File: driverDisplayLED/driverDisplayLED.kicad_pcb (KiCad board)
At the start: 2 copper layers, 59 parts, among them J1 Conn_01x12_Male, J10 Conn_01x12_Male, J11 Conn_01x12_Male, J12 Conn_01x12_Male, J13 Conn_01x12_Male, J14 Conn_01x12_Male, J15 Conn_01x12_Male, J16 Conn_01x12_Male, J17 Conn_01x12_Male, J2 Conn_01x12_Male, J3 Conn_01x12_Male, J4 Conn_02x08_Counter_Clockwise, J5 Conn_01x12_Male, J6 Conn_01x12_Male, J7 Conn_01x12_Male, J8 Conn_01x12_Male, J9 Conn_01x12_Male, Q1 FDS4953, Q2 FDS4953, Q3 FDS4953, Q4 FDS4953, Q5 FDS4953, Q6 FDS4953, Q7 FDS4953, Q8 FDS4953, U1 74HC245, U2 74HC595, U3 74HC595, U4 74HC245, U5 74HC138D, U6 74HC04, U7 74HC595, U8 74HC595, U9 74HC138D

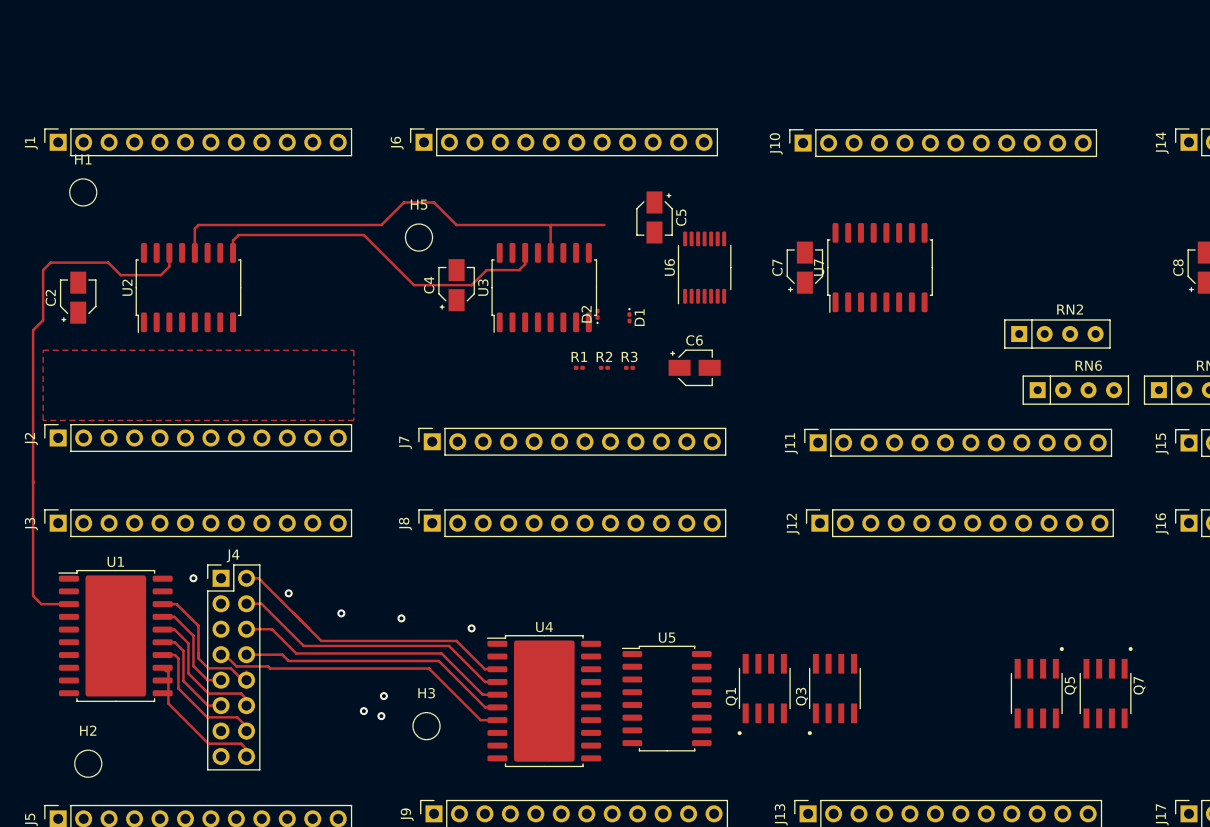
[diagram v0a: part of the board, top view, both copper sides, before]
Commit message: footprint matrix + vias primer bloque
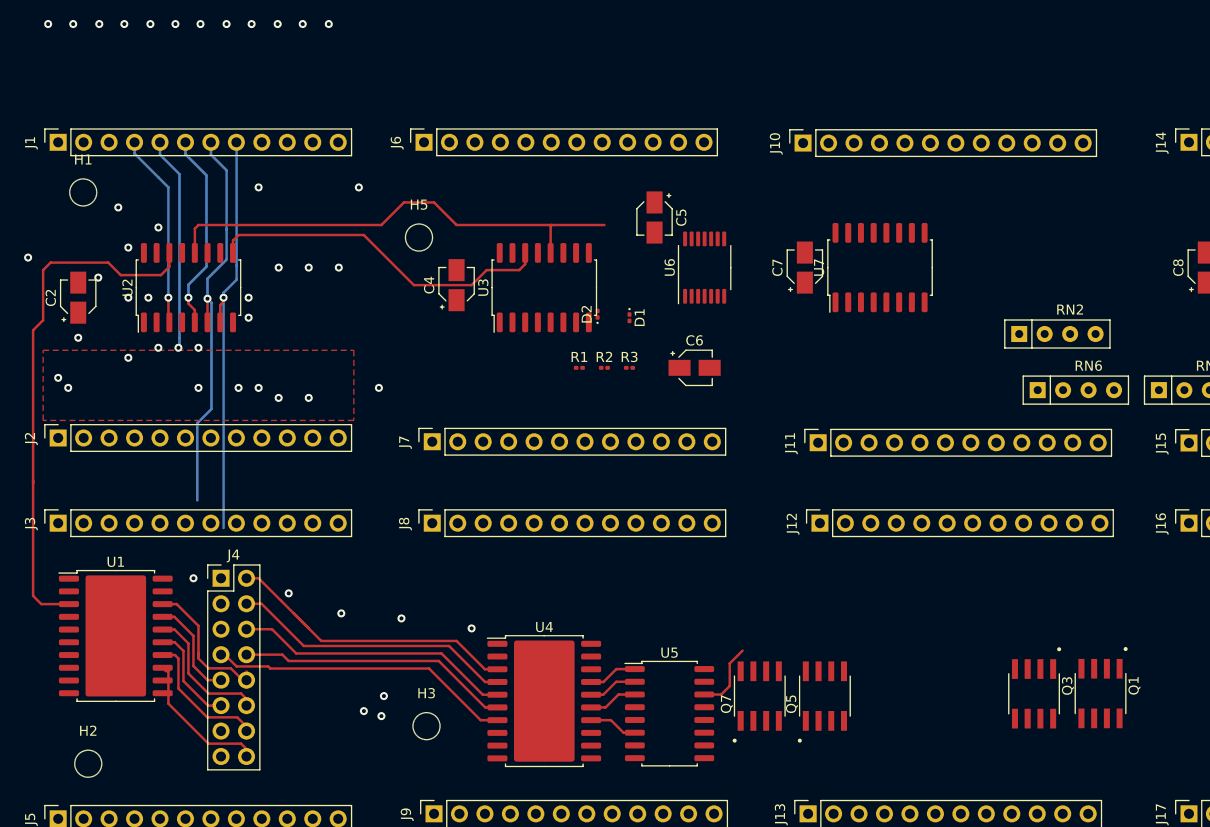
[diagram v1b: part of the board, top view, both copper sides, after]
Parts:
- moved Q7 34.5 mm to (133.0, 117.8), turned to 90 degrees
- moved Q1 33.5 mm to (167.0, 117.5), turned to 270 degrees
- moved Q5 21.1 mm to (139.5, 117.8), turned to 90 degrees
- moved Q3 19.9 mm to (160.4, 117.5), turned to 270 degrees
- moved U5 1.52 mm to (124.0, 119.5)
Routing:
- net /L1R1: track 0.00 -> 41.6 mm, vias 0 -> 2
- net /L1R2: track 0.00 -> 40.3 mm, vias 0 -> 1
- net /L1R4: track 0.00 -> 21.3 mm, vias 0 -> 2
- net /L1R3: track 0.00 -> 19.8 mm, vias 0 -> 2
- net /L1R5: track 0.00 -> 19.4 mm, vias 0 -> 2
- net /Y1-G1b: track 0.00 -> 6.95 mm
- net Net-(U4-Pad15): track 0.00 -> 4.90 mm
- net Net-(U4-Pad17): track 0.00 -> 4.90 mm
- net Net-(U4-Pad16): track 0.00 -> 4.90 mm
- net Net-(U4-Pad14): track 0.00 -> 4.88 mm
- net /L1R8: vias 0 -> 1
- net /L1R7: vias 0 -> 1
- net /L1R6: vias 0 -> 1
- net /H4a: vias 0 -> 1
- net /H3a: vias 0 -> 1
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
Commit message: Esquemático actualizado, encapsulados de capacitores actualizados, footprints de prueba de las matrices led, vias
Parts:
- added J19: Conn_01x02_Female, Connector_Phoenix_MC:PhoenixContact_MCV_1,5_2-GF-3.5_1x02_P3.50mm_Vertical_ThreadedFlange_MountHole, F.Cu at (218.0, 109.0)
- added L1: LedMatrix_M, myLedMatrixFootprint:1588AB-24, F.Cu at (204.2, 98.2)
- added L2: LedMatrix_M, myLedMatrixFootprint:1588AB-24, F.Cu at (243.2, 59.2)
- added L3: LedMatrix_M, myLedMatrixFootprint:1588AB-24, F.Cu at (243.2, 98.2)
- added L4: LedMatrix_M, myLedMatrixFootprint:1588AB-24, F.Cu at (282.1, 59.2)
- added L5: LedMatrix_M, myLedMatrixFootprint:1588AB-24, F.Cu at (204.2, 59.2)
- added L6: LedMatrix_M, myLedMatrixFootprint:1588AB-24, F.Cu at (321.0, 98.2)
- added L7: LedMatrix_M, myLedMatrixFootprint:1588AB-24, F.Cu at (321.0, 59.2)
- added L8: LedMatrix_M, myLedMatrixFootprint:1588AB-24, F.Cu at (282.1, 98.2)
- added U10: 74HC04, Package_SO:TSSOP-14_4.4x5mm_P0.65mm, F.Cu at (207.9, 139.6)
- C1, C11, C2, C3, C4, C5, C6, C7, C8: footprint Capacitor_SMD:CP_Elec_3x5.3 -> Capacitor_SMD:C_0201_0603Metric
- moved C5 112.5 mm to (207.4, 143.7), turned to 0 degrees
- moved R1 111.6 mm to (209.9, 143.7)
- moved R2 111.5 mm to (212.3, 143.7)
- moved R3 111.5 mm to (214.8, 143.7)
- moved U6 110.1 mm to (216.6, 139.6), turned to 0 degrees
- moved D2 109.0 mm to (205.0, 143.7), turned to 0 degrees
- moved C6 108.1 mm to (217.2, 143.7)
- moved D1 107.3 mm to (205.0, 145.5), turned to 0 degrees
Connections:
- D1 pad 2: Net-(D1-Pad2) -> GND
- R1 pad 2: Net-(D1-Pad2) -> Net-(J4-Pad2)
- R2 pad 1: Net-(C6-Pad1) -> Net-(R1-Pad1)
- R2 pad 2: Net-(R1-Pad1) -> GND
- R3 pad 2: Net-(D1-Pad2) -> GND
- U1 pad 8: Net-(RN2-Pad5) -> Net-(RN2-Pad2)
- U6 pad 1: Net-(C6-Pad1) -> (no net)
- U6 pad 2: Net-(C5-Pad1) -> (no net)
- U6 pad 3: Net-(C6-Pad1) -> (no net)
- U6 pad 4: /E1 -> (no net)
- U6 pad 5: /E1 -> (no net)
- U6 pad 6: /E3 -> (no net)
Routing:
- net /L1R6: track 0.00 -> 21.2 mm, vias 1 -> 2
- net /L1R7: track 0.00 -> 10.2 mm, vias 1 -> 2
- net /L1R5: track 19.4 -> 25.4 mm
- net (no net): vias 46 -> 44

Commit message: place and route++
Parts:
- removed U6: 74HC04, Package_SO:TSSOP-14_4.4x5mm_P0.65mm
- U10: footprint Package_SO:TSSOP-14_4.4x5mm_P0.65mm -> Package_SO:SO-14_5.3x10.2mm_P1.27mm
- moved L5 216.4 mm to (-12.0, 68.0)
- moved D1 108.0 mm to (120.7, 78.0), turned to 270 degrees
- moved C6 107.1 mm to (127.8, 84.7)
- moved R2 107.1 mm to (122.9, 84.7)
- moved R1 107.1 mm to (120.5, 84.7)
- moved R3 107.1 mm to (125.4, 84.7)
- moved C5 105.8 mm to (124.5, 78.0), turned to 270 degrees
- moved D2 105.5 mm to (122.5, 78.0), turned to 270 degrees
- moved U10 99.0 mm to (132.2, 75.8), turned to 90 degrees
- moved U7 5.62 mm to (150.6, 75.5)
- moved J1 1.45 mm to (63.1, 64.0)
- moved J10 1.25 mm to (137.3, 63.8)
- moved J14 1.25 mm to (175.8, 63.8)
- moved J6 1.25 mm to (99.5, 63.8)
- moved J11 1.00 mm to (138.8, 91.5)
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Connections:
- U10 pad 14: (no net) -> VCC
- U10 pad 7: (no net) -> GND
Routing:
- net (no net): track 0.00 -> 624.2 mm
- net /H5a: track 0.00 -> 147.2 mm, vias 0 -> 6
- net /H6a: track 0.00 -> 140.0 mm, vias 0 -> 6
- net /H7a: track 0.00 -> 132.5 mm, vias 0 -> 6
- net /H2a: track 0.00 -> 129.8 mm, vias 1 -> 0
- net /H4b: track 0.00 -> 127.4 mm
- net /H2b: track 0.00 -> 126.2 mm
- net /H4a: track 0.00 -> 124.8 mm, vias 1 -> 0
- net /H8a: track 0.00 -> 124.7 mm
- net /H3b: track 0.00 -> 124.5 mm, vias 0 -> 6
- net /H1b: track 0.00 -> 122.5 mm
- net /H7b: track 0.00 -> 120.5 mm
- net /H1a: track 0.00 -> 117.6 mm, vias 1 -> 0
- net /L1R1: track 41.6 -> 29.3 mm, vias 2 -> 1
- net /L1R7: track 10.2 -> 2.84 mm, vias 2 -> 1
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- removed copper zone on F.Cu, net GND
